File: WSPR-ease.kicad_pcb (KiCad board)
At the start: 4 copper layers, 99 x 64 mm, 123 parts, among them J101 GNSS Ant, J102 Tx Ant, J103 pwr+data, Q101 MMBF170, Q301 MMBF170, Q302 MMBF170, Q303 MMBF170, Q304 MMBF170, Q305 MMBF170, Q306 MMBF170, Q307 MMBF170, Q308 MMBF170, Q309 MMBF170, Q310 MMBF170, Q311 MMBF170, Q312 MMBF170, T301 BN-43-202_DualPri_CTSec, U101 ATGM336H-5N31, U102 ESP32-S3-WROOM-1-N8R8, U103 TPS22918DBVR, U104 TPS74612PQWDRBRQ1, U105 SRV05-4, U106 LMR51430, U201 AS183-92LF, U202 AS183-92LF, U203 AS183-92LF, U204 AS183-92LF, U301 ICE40UP5K-SG48ITR, U302 CD74ACT541SM96, Y301 40MHz

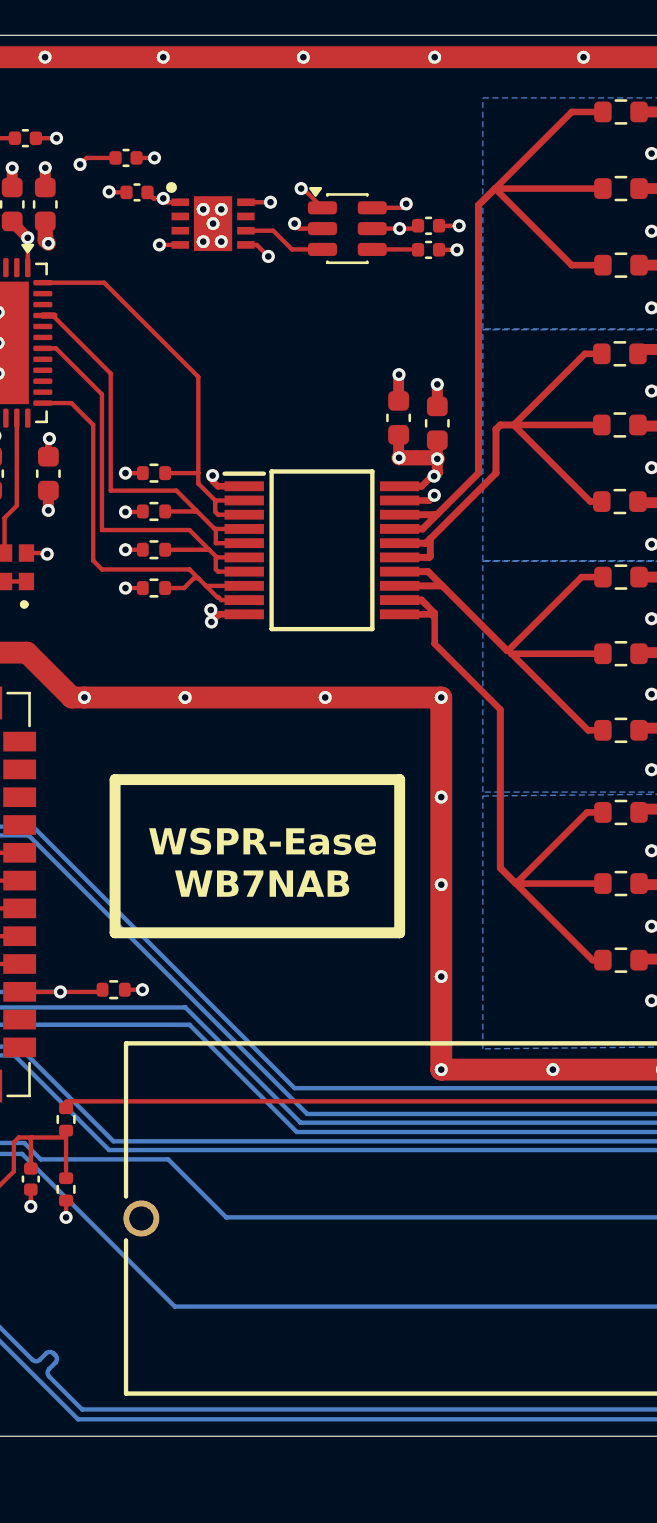
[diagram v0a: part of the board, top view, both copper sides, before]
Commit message: Small changes to part numbers to ease supply chain issues for build
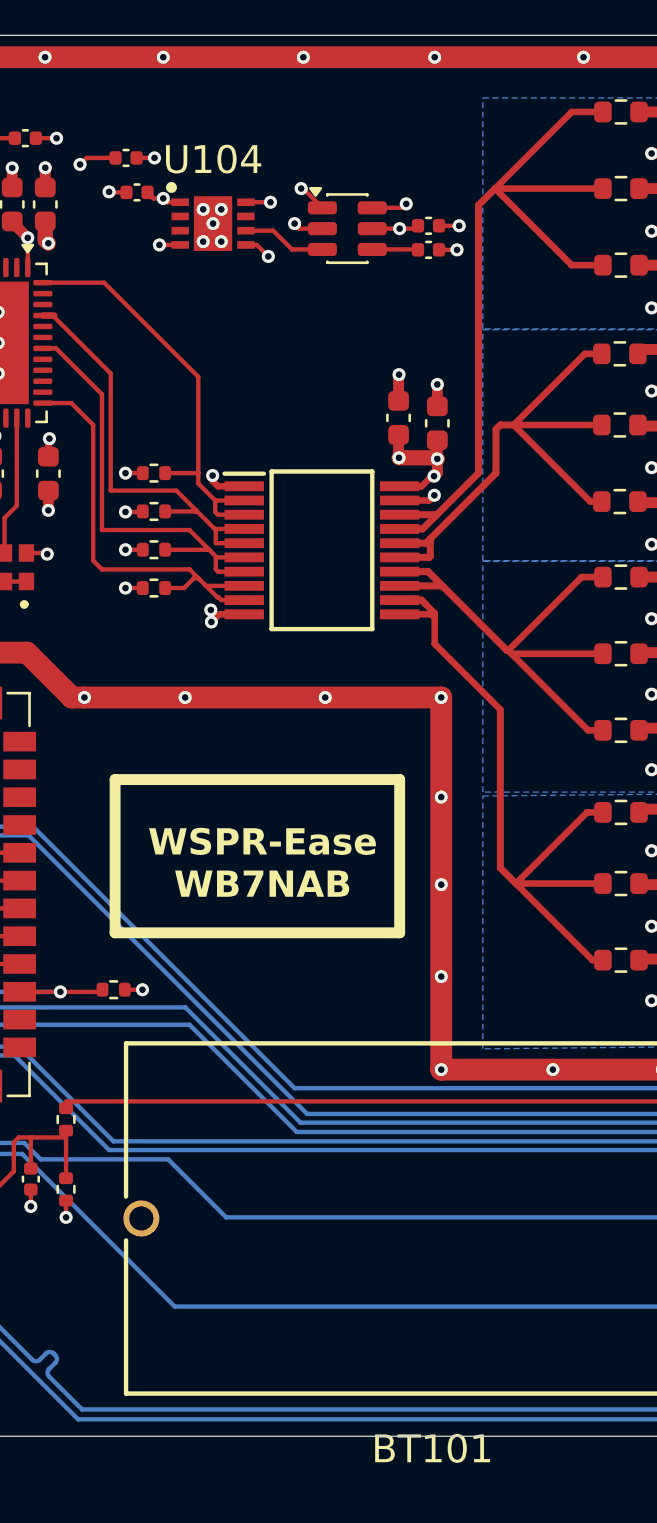
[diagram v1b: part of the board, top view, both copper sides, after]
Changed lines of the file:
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@@
 			)
 		)
-		(property "LCSC" "C703714"
+		(property "LCSC" "C2044063"
 			(at 0 0 270)
 			(unlocked yes)
@@
 			(at 13.8 -9.3 180)
 			(layer "F.SilkS")
-			(hide yes)
 			(effects
 				(font
@@
 			)
 		)
-		(property "LCSC" "C31226699"
+		(property "LCSC" "C6750449"
 			(at 0 0 180)
 			(unlocked yes)
@@
 			)
 		)
-		(property "LCSC" "C703714"
+		(property "LCSC" "C2044063"
 			(at 0 0 0)
 			(unlocked yes)
@@
 			(at 0 -2.9 0)
 			(layer "F.SilkS")
-			(hide yes)
 			(effects
 				(font
@@
 		)
 		(embedded_fonts no)
-		(model "${KIPRJMOD}/symbols/TPS74612PQWDRBRQ1/3D/TPS74612PQWDRBRQ1.stp"
+		(model "TPS74612PQWDRBRQ1.stp"
 			(offset
 				(xyz 0 0 0)

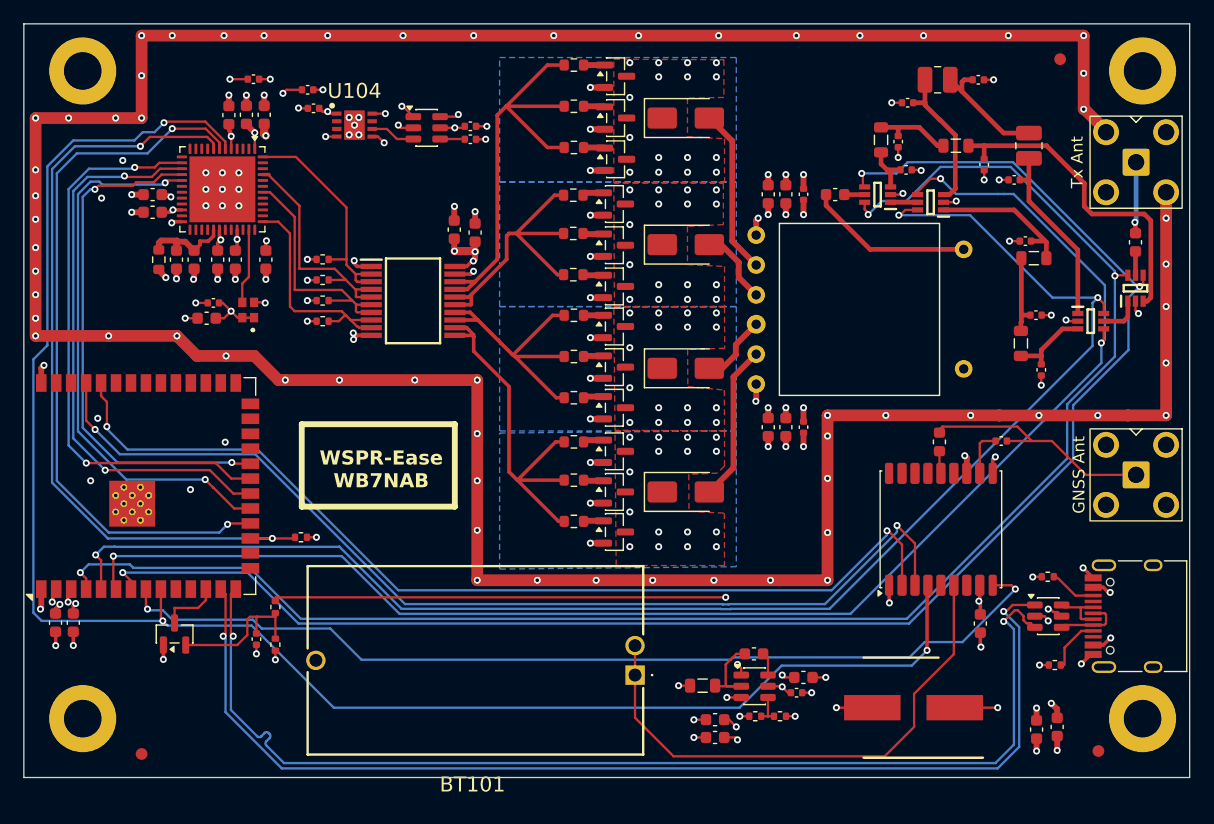
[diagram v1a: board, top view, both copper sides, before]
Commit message: Clean up signal quality and noise incursion into GNSS by moving some traces around
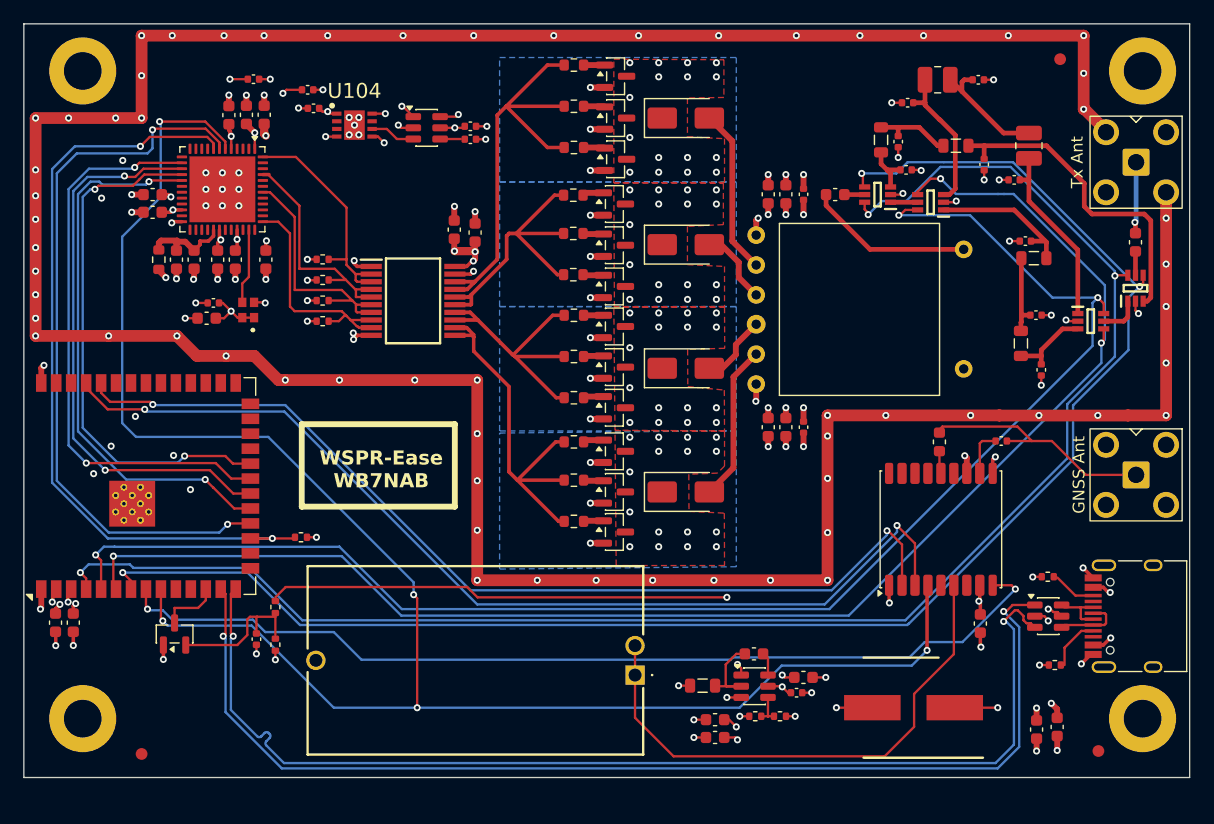
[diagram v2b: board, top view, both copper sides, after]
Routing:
- net /gnssPPS: track 145.9 -> 153.2 mm, vias 3 -> 5
- net /gnssRx: track 87.3 -> 85.7 mm
- net /gnssTx: track 83.5 -> 82.0 mm
- net /fpgaDONE: track 61.1 -> 62.0 mm
- net VBUS: track 60.3 -> 61.2 mm
- net GND: vias 166 -> 167
